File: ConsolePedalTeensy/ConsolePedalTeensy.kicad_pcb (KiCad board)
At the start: 2 copper layers, 100 x 60 mm, 26 parts, among them J1 Conn_02x25_Counter_Clockwise, SW1 SW_Push, SW2 SW_Push, U1 Teensy3.2, U2 LM7805_TO220

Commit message: Finalized traces and exported to gerbers. Should be ready for ordering
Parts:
- moved R11 7.73 mm to (96.5, 87.1)
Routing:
- net Net-(C5-Pad1): track 0.00 -> 187.6 mm
- net Net-(C4-Pad1): track 0.00 -> 107.9 mm
- net Net-(C4-Pad2): track 0.00 -> 96.4 mm
- net Net-(D3-Pad1): track 0.00 -> 79.1 mm
- net +9V: track 60.1 -> 124.6 mm
- net Net-(SW2-Pad2): track 0.00 -> 50.0 mm
- net /Input: track 71.6 -> 110.3 mm
- net Net-(C3-Pad1): track 0.00 -> 38.1 mm
- net Net-(R6-Pad1): track 0.00 -> 35.2 mm
- net Net-(SW1-Pad2): track 0.00 -> 31.3 mm
- net Net-(D4-Pad1): track 0.00 -> 29.5 mm
- net Net-(RV1-Pad2): track 0.00 -> 28.6 mm
- net Net-(R5-Pad1): track 0.00 -> 28.3 mm
- net Net-(R2-Pad1): track 0.00 -> 23.6 mm
- net GND: track 102.5 -> 126.0 mm, vias 4 -> 7
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- added copper zone on F.Cu, net GND

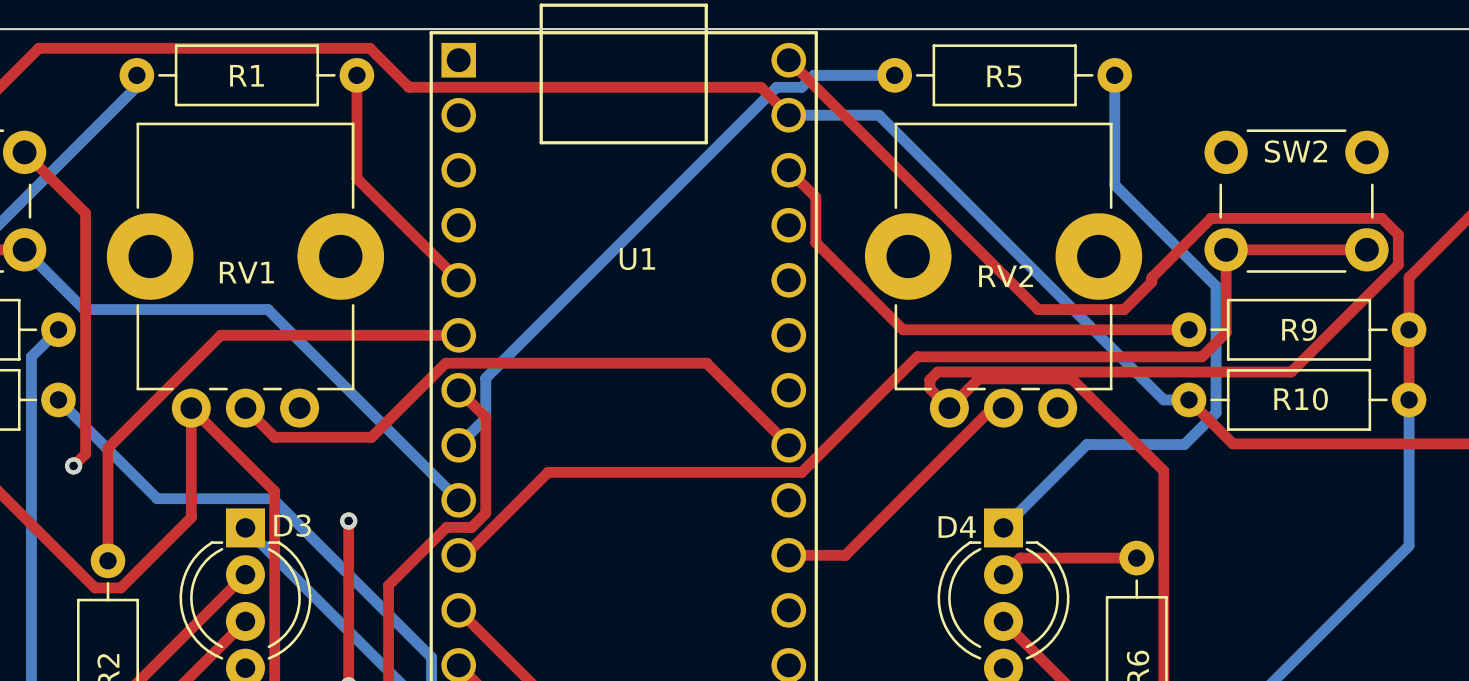
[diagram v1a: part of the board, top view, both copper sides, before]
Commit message: Fixed minor issues with silkscreen
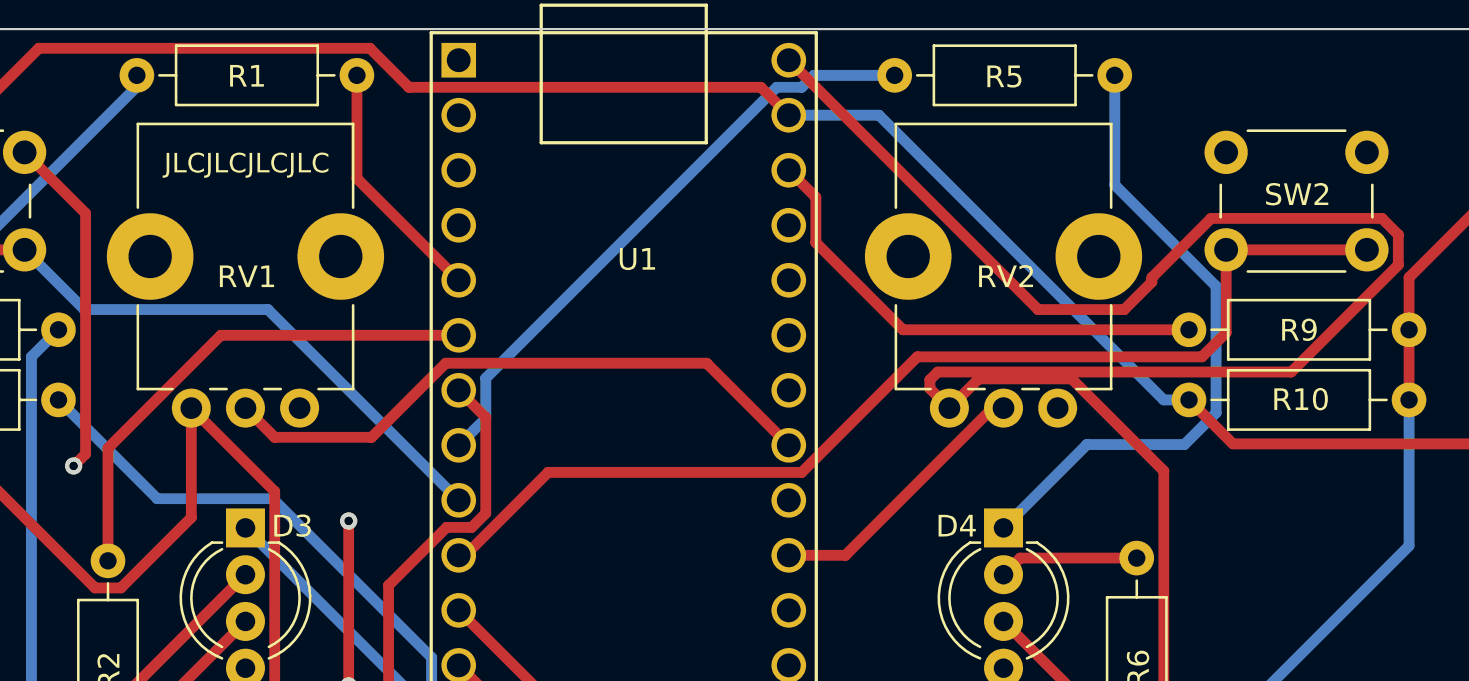
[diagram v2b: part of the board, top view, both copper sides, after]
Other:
- board text added: "JLCJLCJLCJLC"
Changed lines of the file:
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@@
   (general
     (thickness 1.6)
-    (drawings 32)
+    (drawings 33)
     (tracks 210)
     (zones 0)
@@
   (layers
     (0 F.Cu signal)
-    (31 B.Cu signal)
+    (31 B.Cu signal hide)
     (32 B.Adhes user)
     (33 F.Adhes user)
@@
     (descr "LED, diameter 5.0mm, 2 pins, diameter 5.0mm, 3 pins, diameter 5.0mm, 4 pins, http://www.kingbright.com/attachments/file/psearch/000/00/00/L-154A4SUREQBFZGEW(Ver.9A).pdf")
     (tags "LED diameter 5.0mm 2 pins diameter 5.0mm 3 pins diameter 5.0mm 4 pins RGB RGBLED")
-    (fp_text reference D4 (at -0.004 2.168 180) (layer F.SilkS)
+    (fp_text reference D4 (at -0.0675 2.168 180) (layer F.SilkS)
       (effects (font (size 1 1) (thickness 0.15)))
     )
@@
     (descr "Potentiometer, vertical, Bourns PTV09A-1 Single, http://www.bourns.com/docs/Product-Datasheets/ptv09.pdf")
     (tags "Potentiometer vertical Bourns PTV09A-1 Single")
-    (fp_text reference RV1 (at 6.22 -2.434 180) (layer F.SilkS)
+    (fp_text reference RV1 (at 6.05 -2.434 180) (layer F.SilkS)
       (effects (font (size 1 1) (thickness 0.15)))
     )
@@
     (descr https://www.omron.com/ecb/products/pdf/en-b3f.pdf)
     (tags "tact sw push 6mm")
-    (fp_text reference SW2 (at 3.25 0) (layer F.SilkS)
+    (fp_text reference SW2 (at 3.302 1.9685) (layer F.SilkS)
       (effects (font (size 1 1) (thickness 0.15)))
     )
@@
     )
   )
+  (gr_text JLCJLCJLCJLC (at 115.316 76.2) (layer F.SilkS)
+    (effects (font (size 0.9 0.9) (thickness 0.15)))
+  )
   (gr_line (start 182 70) (end 83.3 70) (layer Edge.Cuts) (width 0.1))
